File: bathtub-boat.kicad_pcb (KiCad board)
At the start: 2 copper layers, 61 x 35 mm, 54 parts, among them J1 I2C, J2 SPI, J3 I2C, J4 DS18B20, J5 1WireTRS, SW1 MODE, SW2 RESET, SW3 POWER, SW4 A, U1 esp-01m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

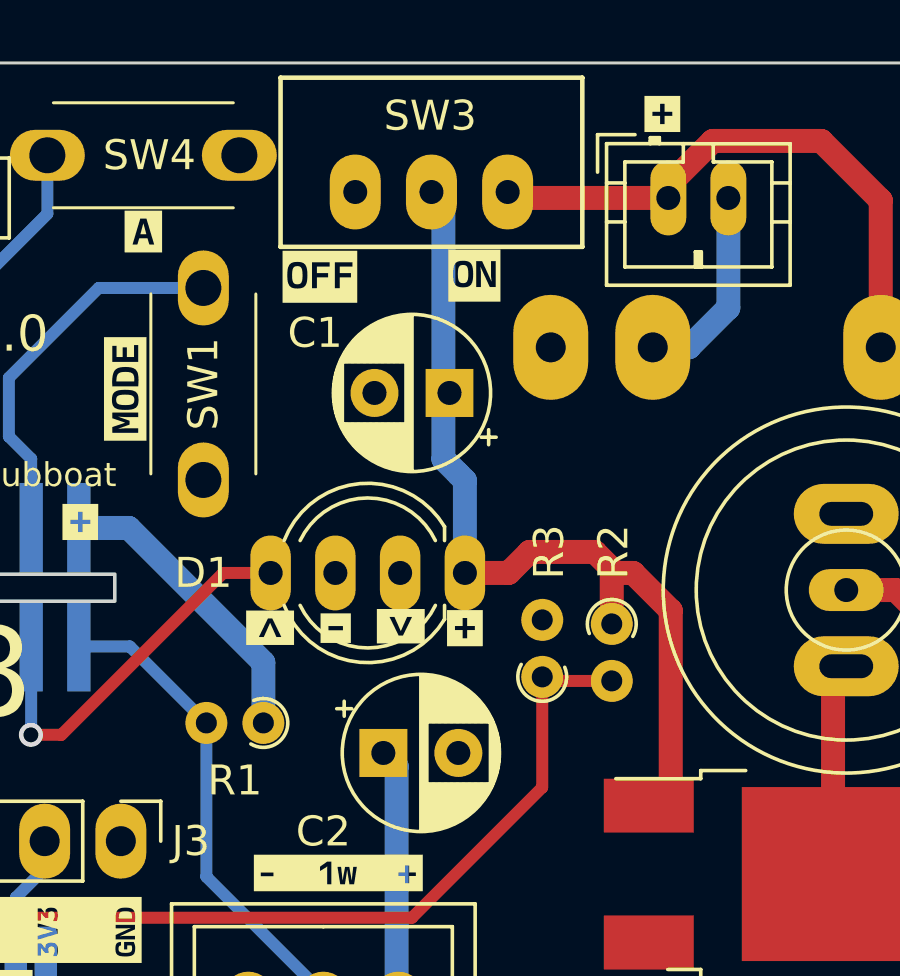
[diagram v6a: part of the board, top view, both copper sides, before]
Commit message: Use special Play-Zone NeoPixel which has a different layout
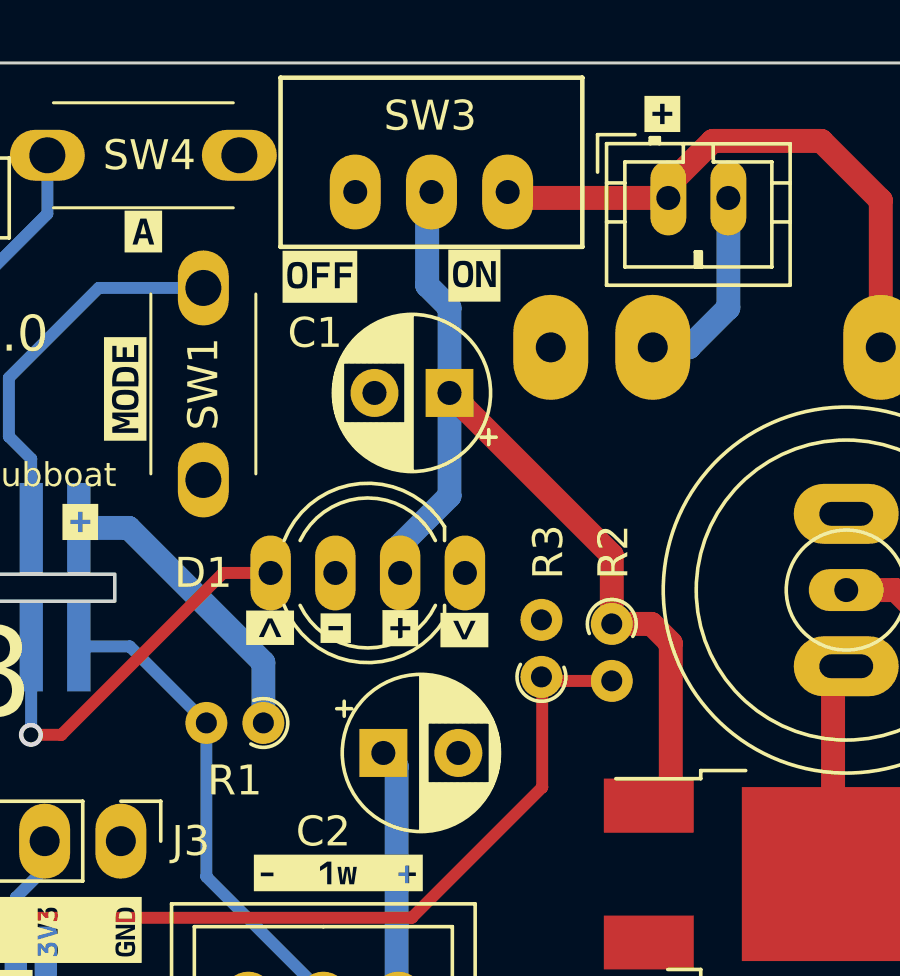
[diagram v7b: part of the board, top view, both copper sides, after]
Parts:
- D1: value WS2812B -> NeoPixel BY Play-Zone.ch
- moved kibuzzard-65B795B9 2.15 mm to (138.1, 84.3), turned to 180 degrees
- moved kibuzzard-679F7FF7 2.12 mm to (140.2, 84.4)
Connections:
- D1 pad 1: +5V -> unconnected-(D1-DOUT-Pad1)
- D1 pad 2: unconnected-(D1-DOUT-Pad2) -> +5V
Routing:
- net +5V: track 30.0 -> 31.9 mm
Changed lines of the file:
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@@
   (net 0 "")
   (net 1 "GND")
-  (net 2 "unconnected-(D1-DOUT-Pad2)")
+  (net 2 "unconnected-(D1-DOUT-Pad1)")
   (net 3 "+3V3")
   (net 4 "TX")
@@
   (net 22 "ADC")
   (footprint "kibuzzard-679F7FF7" (layer "F.Cu")
-    (at 138.081631 84.276123 -90)
+    (at 140.202742 84.403877 -90)
     (descr "Generated with KiBuzzard")
     (tags "kb_params=eyJBbGlnbm1lbnRDaG9pY2UiOiAiUmlnaHQiLCAiQ2FwTGVmdENob2ljZSI6ICJbIiwgIkNhcFJpZ2h0Q2hvaWNlIjogIl0iLCAiRm9udENvbWJvQm94IjogIkJlcmtlbGV5TW9uby1Cb2xkIiwgIkhlaWdodEN0cmwiOiAiLjgiLCAiTGF5ZXJDb21ib0JveCI6ICJGLlNpbGtTIiwgIk11bHRpTGluZVRleHQiOiAiPiIsICJQYWRkaW5nQm90dG9tQ3RybCI6ICI4IiwgIlBhZGRpbmdMZWZ0Q3RybCI6ICI1IiwgIlBhZGRpbmdSaWdodEN0cmwiOiAiNSIsICJQYWRkaW5nVG9wQ3RybCI6ICI4IiwgIldpZHRoQ3RybCI6ICIifQ==")
@@
         (effects (font (size 1 1) (thickness 0.15)))
     )
-    (fp_text value "WS2812B" (at 3.2385 3.96) (layer "F.Fab")
+    (fp_text value "NeoPixel BY Play-Zone.ch" (at 3.2385 3.96) (layer "F.Fab")
         (effects (font (size 1 1) (thickness 0.15)))
     )
@@
       (stroke (width 0.1) (type solid)) (fill none) (layer "F.Fab"))
     (pad "1" thru_hole oval (at 0 0 270) (size 2.5 1.35) (drill 0.8) (layers "*.Cu" "*.Mask")
-      (net 6 "+5V") (pinfunction "VDD") (pintype "power_in"))
+      (net 2 "unconnected-(D1-DOUT-Pad1)") (pinfunction "DOUT") (pintype "output+no_connect"))
     (pad "2" thru_hole oval (at 2.159 0 270) (size 2.5 1.35) (drill 0.8) (layers "*.Cu" "*.Mask")
-      (net 2 "unconnected-(D1-DOUT-Pad2)") (pinfunction "DOUT") (pintype "output+no_connect"))
+      (net 6 "+5V") (pinfunction "VDD") (pintype "power_in"))
     (pad "3" thru_hole oval (at 4.318 0 270) (size 2.5 1.35) (drill 0.8) (layers "*.Cu" "*.Mask")
       (net 1 "GND") (pinfunction "VSS") (pintype "power_in"))
@@
   )
   (footprint "Resistor_THT:R_Axial_DIN0204_L3.6mm_D1.6mm_P1.90mm_Vertical" (layer "F.Cu")
-    (at 142.796702 85.964673 90)
+    (at 142.77 85.964673 90)
     (descr "Resistor, Axial_DIN0204 series, Axial, Vertical, pin pitch=1.9mm, 0.167W, length*diameter=3.6*1.6mm^2, http://cdn-reichelt.de/documents/datenblatt/B400/1_4W%23YAG.pdf")
     (tags "Resistor Axial_DIN0204 series Axial Vertical pin pitch 1.9mm 0.167W length 3.6mm diameter 1.6mm")
@@
   )
   (footprint "kibuzzard-65B795B9" (layer "F.Cu")
-    (at 140.218907 84.34)
+    (at 138.065466 84.34 180)
     (descr "Generated with KiBuzzard")
     (tags "kb_params=eyJBbGlnbm1lbnRDaG9pY2UiOiAiUmlnaHQiLCAiQ2FwTGVmdENob2ljZSI6ICJbIiwgIkNhcFJpZ2h0Q2hvaWNlIjogIl0iLCAiRm9udENvbWJvQm94IjogIkJlcmtlbGV5TW9uby1Cb2xkIiwgIkhlaWdodEN0cmwiOiAiLjgiLCAiTGF5ZXJDb21ib0JveCI6ICJGLlNpbGtTIiwgIk11bHRpTGluZVRleHQiOiAiKyIsICJQYWRkaW5nQm90dG9tQ3RybCI6ICI1IiwgIlBhZGRpbmdMZWZ0Q3RybCI6ICI1IiwgIlBhZGRpbmdSaWdodEN0cmwiOiAiNSIsICJQYWRkaW5nVG9wQ3RybCI6ICI1IiwgIldpZHRoQ3RybCI6ICIifQ==")
@@
   (segment (start 152.49 92.377319) (end 152.49 86.05) (width 0.8) (layer "F.Cu") (net 1))
   (segment (start 152.649673 92.536992) (end 152.49 92.377319) (width 0.8) (layer "F.Cu") (net 1))
+  (segment (start 139.919 81.919) (end 140 82) (width 0.4) (layer "B.Cu") (net 2))
   (via (at 111.02 79.26) (size 0.8) (drill 0.5) (layers "F.Cu" "B.Cu") (net 3))
   (via (at 104.5 89.5) (size 0.8) (drill 0.5) (layers "F.Cu" "B.Cu") (net 3))
@@
   (segment (start 116.97925 75.763002) (end 110.309598 75.763002) (width 0.4) (layer "B.Cu") (net 5))
   (segment (start 108.509152 77.563448) (end 103.65827 77.563448) (width 0.4) (layer "B.Cu") (net 5))
-  (segment (start 142.374369 81.8) (end 144.548 81.8) (width 0.8) (layer "F.Cu") (net 6))
-  (segment (start 145.248 82.5) (end 145.114601 82.633399) (width 0.8) (layer "F.Cu") (net 6))
+  (segment (start 146.438731 84.198731) (end 145.114601 84.198731) (width 0.8) (layer "F.Cu") (net 6))
   (segment (start 146.349673 90.256992) (end 147.079755 89.52691) (width 0.8) (layer "F.Cu") (net 6))
-  (segment (start 144.548 81.8) (end 145.248 82.5) (width 0.8) (layer "F.Cu") (net 6))
-  (segment (start 147.079755 83.754418) (end 145.825337 82.5) (width 0.8) (layer "F.Cu") (net 6))
   (segment (start 146.19 90.097319) (end 146.349673 90.256992) (width 0.8) (layer "F.Cu") (net 6))
-  (segment (start 147.079755 89.52691) (end 147.079755 83.754418) (width 0.8) (layer "F.Cu") (net 6))
-  (segment (start 145.825337 82.5) (end 145.248 82.5) (width 0.8) (layer "F.Cu") (net 6))
-  (segment (start 141.674369 82.5) (end 142.374369 81.8) (width 0.8) (layer "F.Cu") (net 6))
-  (segment (start 140.218907 82.5) (end 141.674369 82.5) (width 0.8) (layer "F.Cu") (net 6))
-  (segment (start 145.114601 82.633399) (end 145.114601 84.198731) (width 0.8) (layer "F.Cu") (net 6))
-  (segment (start 139.919 81.919) (end 140 82) (width 0.4) (layer "B.Cu") (net 6))
-  (segment (start 140 79.2) (end 140.218907 79.418907) (width 0.8) (layer "B.Cu") (net 6))
-  (segment (start 140 79.2) (end 139.500433 78.700433) (width 0.8) (layer "B.Cu") (net 6))
-  (segment (start 139.500433 70.198495) (end 139.103436 69.801498) (width 0.8) (layer "B.Cu") (net 6))
-  (segment (start 139.500433 78.700433) (end 139.500433 70.198495) (width 0.8) (layer "B.Cu") (net 6))
-  (segment (start 140.218907 79.418907) (end 140.218907 82.5) (width 0.8) (layer "B.Cu") (net 6))
+  (segment (start 147.079755 89.52691) (end 147.079755 84.839755) (width 0.8) (layer "F.Cu") (net 6))
+  (segment (start 145.114601 81.909489) (end 139.705112 76.5) (width 0.8) (layer "F.Cu") (net 6))
+  (segment (start 145.114601 84.198731) (end 145.114601 81.909489) (width 0.8) (layer "F.Cu") (net 6))
+  (segment (start 147.079755 84.839755) (end 146.438731 84.198731) (width 0.8) (layer "F.Cu") (net 6))
+  (segment (start 138.059907 81.577907) (end 138.059907 82.5) (width 0.8) (layer "B.Cu") (net 6))
+  (segment (start 139.705112 76.5) (end 139.705112 79.932702) (width 0.8) (layer "B.Cu") (net 6))
+  (segment (start 138.96 69.944934) (end 138.96 72.91) (width 0.8) (layer "B.Cu") (net 6))
+  (segment (start 138.96 72.91) (end 139.705112 73.655112) (width 0.8) (layer "B.Cu") (net 6))
+  (segment (start 139.705112 73.655112) (end 139.705112 76.5) (width 0.8) (layer "B.Cu") (net 6))
+  (segment (start 139.103436 69.801498) (end 138.96 69.944934) (width 0.8) (layer "B.Cu") (net 6))
+  (segment (start 139.705112 79.932702) (end 138.059907 81.577907) (width 0.8) (layer "B.Cu") (net 6))
   (segment (start 125.7625 81) (end 125.7625 78.696667) (width 0.4) (layer "B.Cu") (net 7))
   (segment (start 125.0185 77.952667) (end 125.0185 75.995333) (width 0.4) (layer "B.Cu") (net 7))
@@
   (segment (start 110.5 88.5) (end 107.5 85.5) (width 0.4) (layer "B.Cu") (net 15))
   (segment (start 125.752 87.896) (end 126.768 87.896) (width 0.4) (layer "F.Cu") (net 16))
-  (segment (start 132.164 82.5) (end 133.741907 82.5) (width 0.4) (layer "F.Cu") (net 16))
+  (segment (start 133.741907 82.5) (end 132.164 82.5) (width 0.4) (layer "F.Cu") (net 16))
   (segment (start 126.768 87.896) (end 132.164 82.5) (width 0.4) (layer "F.Cu") (net 16))
   (via (at 125.752 87.896) (size 0.8) (drill 0.5) (layers "F.Cu" "B.Cu") (net 16))
@@
   (segment (start 147.685 74.98) (end 149 73.665) (width 0.8) (layer "B.Cu") (net 21))
   (segment (start 142.796702 89.647298) (end 138.452 93.992) (width 0.4) (layer "F.Cu") (net 22))
-  (segment (start 119.07658 93.992) (end 116.768141 91.683561) (width 0.4) (layer "F.Cu") (net 22))
-  (segment (start 145.114601 86.098731) (end 142.93076 86.098731) (width 0.4) (layer "F.Cu") (net 22))
-  (segment (start 138.452 93.992) (end 119.07658 93.992) (width 0.4) (layer "F.Cu") (net 22))
-  (segment (start 142.93076 86.098731) (end 142.796702 85.964673) (width 0.4) (layer "F.Cu") (net 22))
   (segment (start 116.768141 91.683561) (end 116.768141 87.65) (width 0.4) (layer "F.Cu") (net 22))
-  (segment (start 142.796702 85.964673) (end 142.796702 89.647298) (width 0.4) (layer "F.Cu") (net 22))
+  (segment (start 142.904058 86.098731) (end 142.77 85.964673) (width 0.4) (layer "F.Cu") (net 22))
+  (segment (start 145.114601 86.098731) (end 142.904058 86.098731) (width 0.4) (layer "F.Cu") (net 22))
+  (segment (start 142.77 85.964673) (end 142.796702 85.991375) (width 0.4) (layer "F.Cu") (net 22))
+  (segment (start 138.452 93.992) (end 119.07658 93.992) (width 0.4) (layer "F.Cu") (net 22))
+  (segment (start 142.796702 85.991375) (end 142.796702 89.647298) (width 0.4) (layer "F.Cu") (net 22))
+  (segment (start 119.07658 93.992) (end 116.768141 91.683561) (width 0.4) (layer "F.Cu") (net 22))
   (via (at 116.768141 87.65) (size 0.8) (drill 0.5) (layers "F.Cu" "B.Cu") (net 22))
   (segment (start 117.825 86.593141) (end 116.768141 87.65) (width 0.4) (layer "B.Cu") (net 22))

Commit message: Final preparations for production
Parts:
- moved G*** 11.4 mm to (115.3, 94.6)
- moved kibuzzard-65B796FD 9.84 mm to (107.5, 70.0)
- moved kibuzzard-65B79597 1.97 mm to (107.2, 89.4)
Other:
- board text added: "Bathtubboat v2.0 4.02.2025 @abcdef"
- board text removed: "Bathtubboat v2.0 22.02.2024"
- board text removed: "WARNING: Wiring of Neopixel is different"
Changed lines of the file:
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@@
   )
   (footprint "kibuzzard-65B79597" (layer "F.Cu")
-    (at 109.140179 89.026234)
+    (at 107.21 89.42)
     (descr "Generated with KiBuzzard")
     (tags "kb_params=eyJBbGlnbm1lbnRDaG9pY2UiOiAiUmlnaHQiLCAiQ2FwTGVmdENob2ljZSI6ICJbIiwgIkNhcFJpZ2h0Q2hvaWNlIjogIl0iLCAiRm9udENvbWJvQm94IjogIkJlcmtlbGV5TW9uby1Cb2xkIiwgIkhlaWdodEN0cmwiOiAiLjgiLCAiTGF5ZXJDb21ib0JveCI6ICJGLlNpbGtTIiwgIk11bHRpTGluZVRleHQiOiAiUkVTRVQiLCAiUGFkZGluZ0JvdHRvbUN0cmwiOiAiNSIsICJQYWRkaW5nTGVmdEN0cmwiOiAiNSIsICJQYWRkaW5nUmlnaHRDdHJsIjogIjUiLCAiUGFkZGluZ1RvcEN0cmwiOiAiNSIsICJXaWR0aEN0cmwiOiAiIn0=")
@@
     (property "ki_keywords" "mounting hole")
     (attr exclude_from_pos_files)
-    (fp_text reference "H1" (at 0 -4.2) (layer "F.SilkS")
+    (fp_text reference "H1" (at 0 -4.2) (layer "F.SilkS") hide
         (effects (font (size 1 1) (thickness 0.15)))
     )
@@
         (effects (font (size 1 1) (thickness 0.15)))
     )
+    (fp_text user "Play-Zone NP" (at -6.361093 4.51 unlocked) (layer "F.SilkS")
+        (effects (font (size 1 1) (thickness 0.15)))
+    )
     (fp_text user "${REFERENCE}" (at 3.2385 -3.96) (layer "F.Fab")
         (effects (font (size 1 1) (thickness 0.15)))
@@
   )
   (footprint "kibuzzard-65B796FD" (layer "F.Cu")
-    (at 117 72.4)
+    (at 107.45017 70.0133)
     (descr "Generated with KiBuzzard")
     (tags "kb_params=eyJBbGlnbm1lbnRDaG9pY2UiOiAiUmlnaHQiLCAiQ2FwTGVmdENob2ljZSI6ICJbIiwgIkNhcFJpZ2h0Q2hvaWNlIjogIl0iLCAiRm9udENvbWJvQm94IjogIkJlcmtlbGV5TW9uby1Cb2xkIiwgIkhlaWdodEN0cmwiOiAiLjgiLCAiTGF5ZXJDb21ib0JveCI6ICJGLlNpbGtTIiwgIk11bHRpTGluZVRleHQiOiAiU1BJXG4iLCAiUGFkZGluZ0JvdHRvbUN0cmwiOiAiOSIsICJQYWRkaW5nTGVmdEN0cmwiOiAiMyIsICJQYWRkaW5nUmlnaHRDdHJsIjogIjMiLCAiUGFkZGluZ1RvcEN0cmwiOiAiNyIsICJXaWR0aEN0cmwiOiAiIn0=")
@@
   )
   (footprint "LOGO" (layer "F.Cu")
-    (at 104.228102 91.652068)
+    (at 115.251113 94.605278)
     (attr board_only exclude_from_pos_files exclude_from_bom)
     (fp_text reference "G***" (at 0 0) (layer "F.SilkS") hide
@@
     )
   )
+  (gr_line (start 144.84173 78.722864) (end 139.540407 80.955)
+    (stroke (width 0.15) (type default)) (layer "F.SilkS"))
   (gr_arc (start 102.5 100.5) (mid 100.37868 99.62132) (end 99.5 97.5)
     (stroke (width 0.1) (type default)) (layer "Edge.Cuts"))
@@
     (effects (font (size 3 3) (thickness 0.5)) (justify mirror))
   )
-  (gr_text "WARNING: Wiring of Neopixel is different" (at 123.72 62.75) (layer "F.SilkS")
-    (effects (font (size 1 1) (thickness 0.15)) (justify left bottom))
-  )
-  (gr_text "Bathtubboat v2.0\n22.02.2024" (at 119.148 75.5) (layer "F.SilkS")
+  (gr_text "Bathtubboat v2.0\n4.02.2025\n@abcdef" (at 119.148 75.5) (layer "F.SilkS")
     (effects (font (size 1.2 1.2) (thickness 0.2)))
   )
